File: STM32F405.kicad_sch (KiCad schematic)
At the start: 21 parts, among them SW1 SW_MEC_5E, U2 STM32F405RGTx, Y1 Crystal, Y2 Crystal

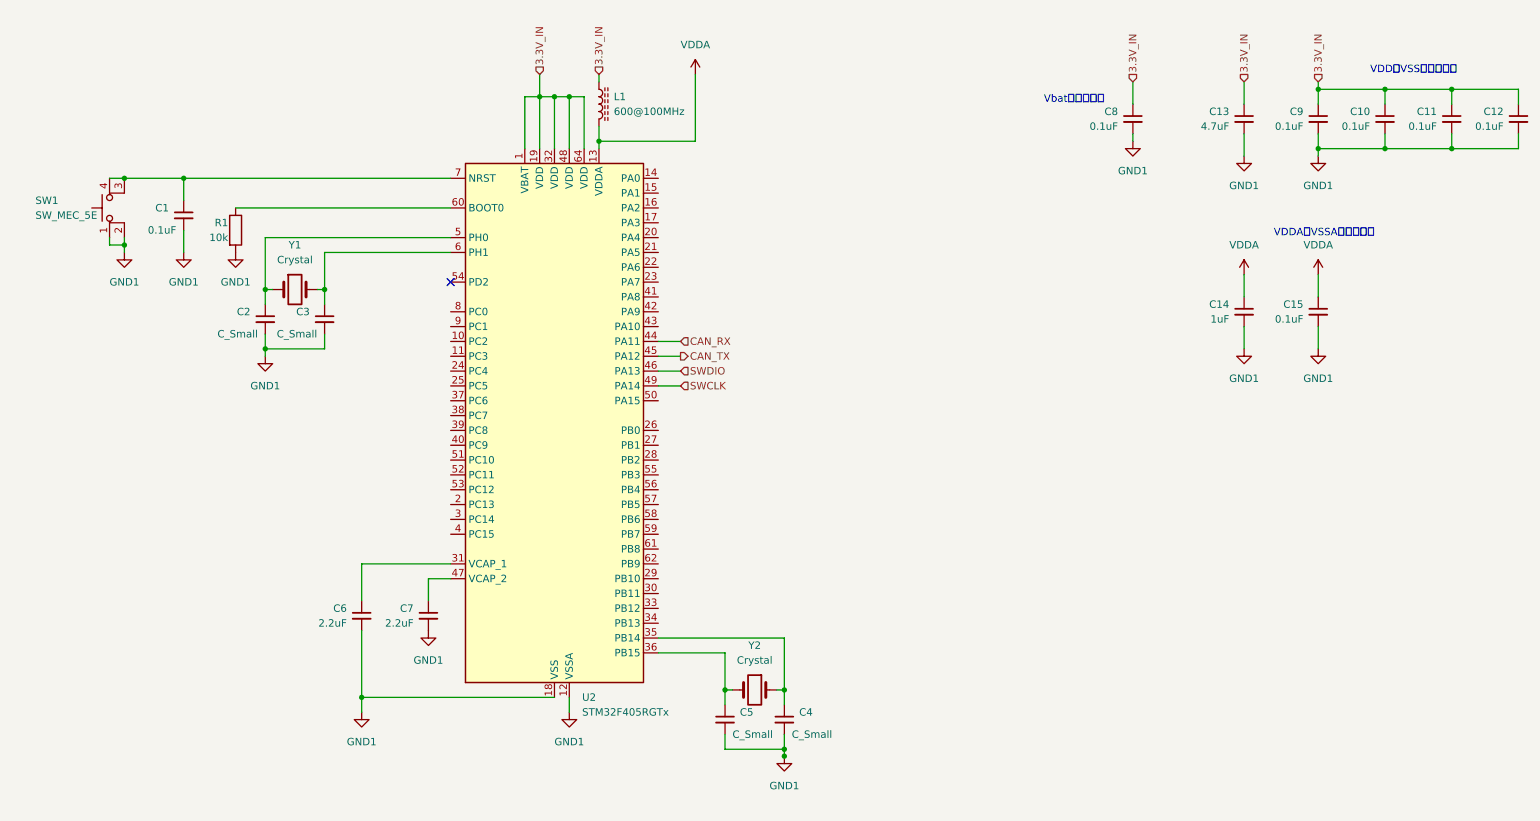
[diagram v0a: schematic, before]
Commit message: update Driver circuit
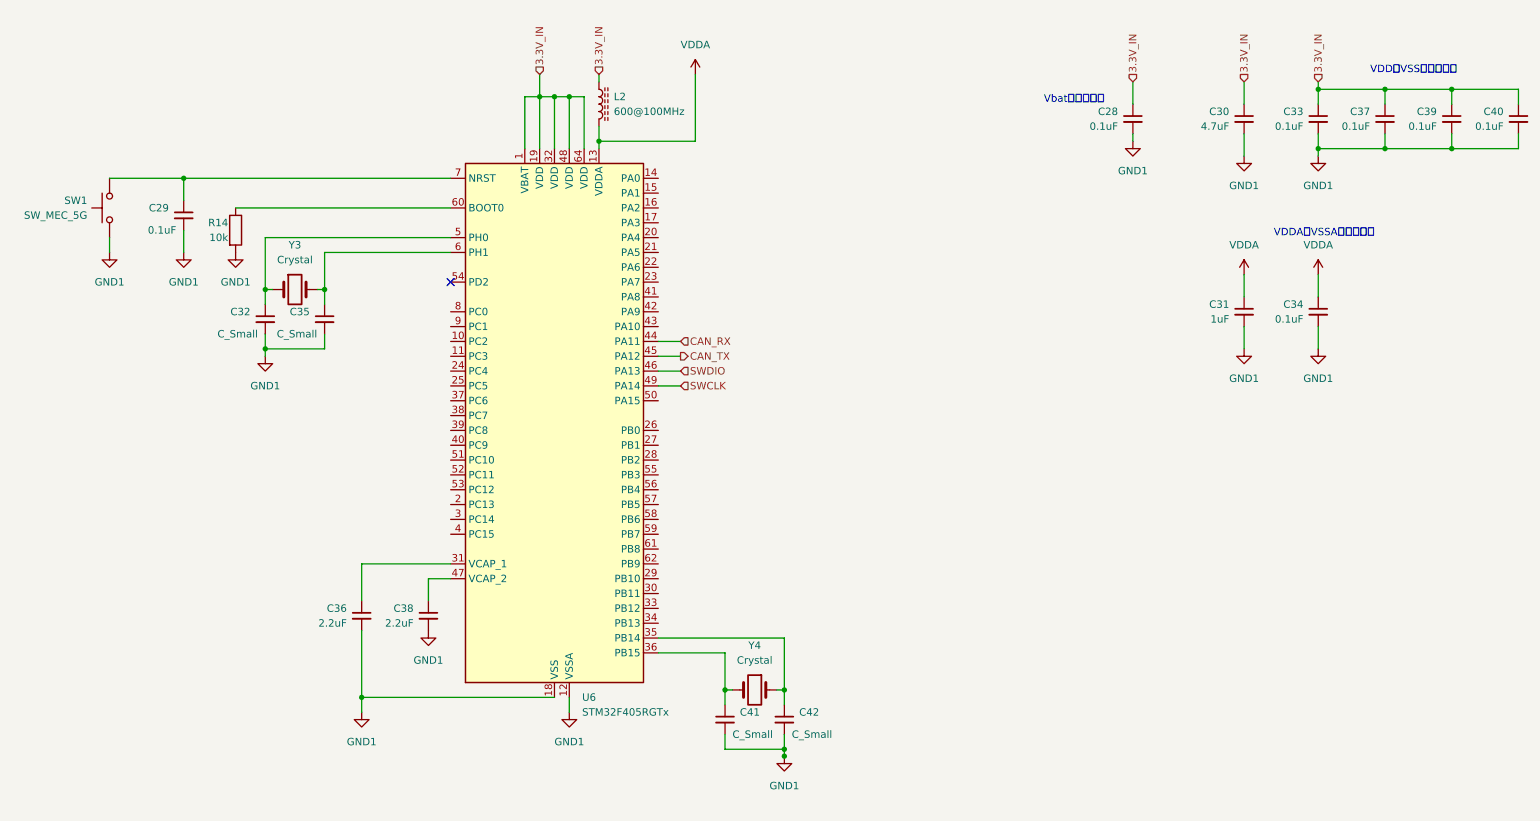
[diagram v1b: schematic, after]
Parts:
- removed SW1: SW_MEC_5E, symbol Switch:SW_MEC_5E
- added SW1: SW_MEC_5G, Button_Switch_THT:SW_PUSH_6mm, symbol Switch:SW_MEC_5G
- renumbered C8 to C28, C1 to C29, C13 to C30, C14 to C31, C2 to C32, C9 to C33, C15 to C34, C3 to C35, C6 to C36, C10 to C37, C7 to C38, C11 to C39, C12 to C40, C5 to C41, C4 to C42, L1 to L2, R1 to R14, U2 to U6, Y1 to Y3, Y2 to Y4
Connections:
- net GND1: now also SW1.1 (A), SW1.2 (A)
- net at C29.1, U6.7 (NRST): now also SW1.3 (B), SW1.4 (B)

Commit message: update parts list
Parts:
- R14: footprint (none) -> Resistor_SMD:R_1206_3216Metric_Pad1.30x1.75mm_HandSolder
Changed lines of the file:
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@@
       (effects (font (size 1.27 1.27)) (justify right))
     )
-    (property "Footprint" "" (at 56.642 53.34 90)
+    (property "Footprint" "Resistor_SMD:R_1206_3216Metric_Pad1.30x1.75mm_HandSolder" (at 56.642 53.34 90)
       (effects (font (size 1.27 1.27)) hide)
     )

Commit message: add footprint
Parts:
- C28, C29, C33, C34, C37, C39, C40: value 0.1uF -> 0.1u
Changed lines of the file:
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@@
       (effects (font (size 1.27 1.27)) (justify right))
     )
-    (property "Value" "0.1uF" (at 48.26 53.34 0)
+    (property "Value" "0.1u" (at 48.26 53.34 0)
       (effects (font (size 1.27 1.27)) (justify right))
     )
@@
       (effects (font (size 1.27 1.27)) (justify right))
     )
-    (property "Value" "0.1uF" (at 241.3 68.58 0)
+    (property "Value" "0.1u" (at 241.3 68.58 0)
       (effects (font (size 1.27 1.27)) (justify right))
     )
@@
       (effects (font (size 1.27 1.27)) (justify right))
     )
-    (property "Value" "0.1uF" (at 252.73 35.56 0)
+    (property "Value" "0.1u" (at 252.73 35.56 0)
       (effects (font (size 1.27 1.27)) (justify right))
     )
@@
       (effects (font (size 1.27 1.27)) (justify right))
     )
-    (property "Value" "0.1uF" (at 209.55 35.56 0)
+    (property "Value" "0.1u" (at 209.55 35.56 0)
       (effects (font (size 1.27 1.27)) (justify right))
     )
@@
       (effects (font (size 1.27 1.27)) (justify right))
     )
-    (property "Value" "0.1uF" (at 264.16 35.56 0)
+    (property "Value" "0.1u" (at 264.16 35.56 0)
       (effects (font (size 1.27 1.27)) (justify right))
     )
@@
       (effects (font (size 1.27 1.27)) (justify right))
     )
-    (property "Value" "0.1uF" (at 275.59 35.56 0)
+    (property "Value" "0.1u" (at 275.59 35.56 0)
       (effects (font (size 1.27 1.27)) (justify right))
     )
@@
       (effects (font (size 1.27 1.27)) (justify right))
     )
-    (property "Value" "0.1uF" (at 241.3 35.56 0)
-      (effects (font (size 1.27 1.27)) (justify right))
-    )
+    (property "Value" "0.1u" (at 241.3 35.56 0)
+      (effects (font (size 1.27 1.27)) (justify right))
+    )

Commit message: Update motor driver circuit
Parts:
- C28, C29, C33, C34, C37, C39, C40: footprint (none) -> Capacitor_SMD:C_01005_0402Metric_Pad0.57x0.30mm_HandSolder
- C30, C31, C36, C38: footprint (none) -> Capacitor_SMD:C_0603_1608Metric_Pad1.08x0.95mm_HandSolder
- L2: footprint (none) -> Resistor_SMD:R_0805_2012Metric_Pad1.20x1.40mm_HandSolder
- R14: footprint Resistor_SMD:R_1206_3216Metric_Pad1.30x1.75mm_HandSolder -> Resistor_SMD:R_0402_1005Metric_Pad0.72x0.64mm_HandSolder
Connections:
- net SWO: now reaches U6.55 (PB3)
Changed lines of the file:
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@@
+    (stroke (width 0) (type default))
+  )
+  (wire (pts (xy 130.81 95.25) (xy 134.62 95.25))
     (stroke (width 0) (type default))
   )
@@
     (effects (font (size 1.27 1.27)) (justify left))
   )
+  (hierarchical_label "SWO" (shape input) (at 134.62 95.25 0) (fields_autoplaced)
+    (effects (font (size 1.27 1.27)) (justify left))
+  )
   (hierarchical_label "SWCLK" (shape input) (at 134.62 80.01 0) (fields_autoplaced)
     (effects (font (size 1.27 1.27)) (justify left))
@@
       (effects (font (size 1.27 1.27)) (justify right))
     )
-    (property "Footprint" "" (at 231.14 34.29 0)
+    (property "Footprint" "Capacitor_SMD:C_0603_1608Metric_Pad1.08x0.95mm_HandSolder" (at 231.14 34.29 0)
       (effects (font (size 1.27 1.27)) hide)
     )
@@
       (effects (font (size 1.27 1.27)) (justify right))
     )
-    (property "Footprint" "" (at 49.53 50.8 0)
+    (property "Footprint" "Capacitor_SMD:C_01005_0402Metric_Pad0.57x0.30mm_HandSolder" (at 49.53 50.8 0)
       (effects (font (size 1.27 1.27)) hide)
     )
@@
       (effects (font (size 1.27 1.27)) (justify right))
     )
-    (property "Footprint" "" (at 243.84 67.31 0)
+    (property "Footprint" "Capacitor_SMD:C_01005_0402Metric_Pad0.57x0.30mm_HandSolder" (at 243.84 67.31 0)
       (effects (font (size 1.27 1.27)) hide)
     )
@@
       (effects (font (size 1.27 1.27)) (justify right))
     )
-    (property "Footprint" "" (at 255.27 34.29 0)
+    (property "Footprint" "Capacitor_SMD:C_01005_0402Metric_Pad0.57x0.30mm_HandSolder" (at 255.27 34.29 0)
       (effects (font (size 1.27 1.27)) hide)
     )
@@
       (effects (font (size 1.27 1.27)) (justify right))
     )
-    (property "Footprint" "" (at 80.01 119.38 0)
+    (property "Footprint" "Capacitor_SMD:C_0603_1608Metric_Pad1.08x0.95mm_HandSolder" (at 80.01 119.38 0)
       (effects (font (size 1.27 1.27)) hide)
     )
@@
       (effects (font (size 1.27 1.27)) (justify right))
     )
-    (property "Footprint" "Resistor_SMD:R_1206_3216Metric_Pad1.30x1.75mm_HandSolder" (at 56.642 53.34 90)
+    (property "Footprint" "Resistor_SMD:R_0402_1005Metric_Pad0.72x0.64mm_HandSolder" (at 56.642 53.34 90)
       (effects (font (size 1.27 1.27)) hide)
     )
@@
       (effects (font (size 1.27 1.27)) (justify right))
     )
-    (property "Footprint" "" (at 212.09 34.29 0)
+    (property "Footprint" "Capacitor_SMD:C_01005_0402Metric_Pad0.57x0.30mm_HandSolder" (at 212.09 34.29 0)
       (effects (font (size 1.27 1.27)) hide)
     )
@@
       (effects (font (size 1.27 1.27)) (justify right))
     )
-    (property "Footprint" "" (at 91.44 119.38 0)
+    (property "Footprint" "Capacitor_SMD:C_0603_1608Metric_Pad1.08x0.95mm_HandSolder" (at 91.44 119.38 0)
       (effects (font (size 1.27 1.27)) hide)
     )
@@
       (effects (font (size 1.27 1.27)) (justify right))
     )
-    (property "Footprint" "" (at 266.7 34.29 0)
+    (property "Footprint" "Capacitor_SMD:C_01005_0402Metric_Pad0.57x0.30mm_HandSolder" (at 266.7 34.29 0)
       (effects (font (size 1.27 1.27)) hide)
     )
@@
       (effects (font (size 1.27 1.27)) (justify right))
     )
-    (property "Footprint" "" (at 278.13 34.29 0)
+    (property "Footprint" "Capacitor_SMD:C_01005_0402Metric_Pad0.57x0.30mm_HandSolder" (at 278.13 34.29 0)
       (effects (font (size 1.27 1.27)) hide)
     )
@@
       (effects (font (size 1.27 1.27)) (justify right))
     )
-    (property "Footprint" "" (at 231.14 67.31 0)
+    (property "Footprint" "Capacitor_SMD:C_0603_1608Metric_Pad1.08x0.95mm_HandSolder" (at 231.14 67.31 0)
       (effects (font (size 1.27 1.27)) hide)
     )
@@
       (effects (font (size 1.27 1.27)) (justify left))
     )
-    (property "Footprint" "" (at 120.65 31.75 0)
+    (property "Footprint" "Resistor_SMD:R_0805_2012Metric_Pad1.20x1.40mm_HandSolder" (at 120.65 31.75 0)
       (effects (font (size 1.27 1.27)) hide)
     )
@@
       (effects (font (size 1.27 1.27)) (justify right))
     )
-    (property "Footprint" "" (at 243.84 34.29 0)
-      (effects (font (size 1.27 1.27)) hide)
-    )
+    (property "Footprint" "Capacitor_SMD:C_01005_0402Metric_Pad0.57x0.30mm_HandSolder" (at 243.84 34.29 0)
+      (effects (font (size 1.27 1.27)) hide)
+    )

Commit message: add logic parts
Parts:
- C28, C29, C33, C34, C37, C39, C40: footprint Capacitor_SMD:C_01005_0402Metric_Pad0.57x0.30mm_HandSolder -> Capacitor_SMD:C_0402_1005Metric_Pad0.74x0.62mm_HandSolder
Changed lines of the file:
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@@
       (effects (font (size 1.27 1.27)) (justify right))
     )
-    (property "Footprint" "Capacitor_SMD:C_01005_0402Metric_Pad0.57x0.30mm_HandSolder" (at 49.53 50.8 0)
+    (property "Footprint" "Capacitor_SMD:C_0402_1005Metric_Pad0.74x0.62mm_HandSolder" (at 49.53 50.8 0)
       (effects (font (size 1.27 1.27)) hide)
     )
@@
       (effects (font (size 1.27 1.27)) (justify right))
     )
-    (property "Footprint" "Capacitor_SMD:C_01005_0402Metric_Pad0.57x0.30mm_HandSolder" (at 243.84 67.31 0)
+    (property "Footprint" "Capacitor_SMD:C_0402_1005Metric_Pad0.74x0.62mm_HandSolder" (at 243.84 67.31 0)
       (effects (font (size 1.27 1.27)) hide)
     )
@@
       (effects (font (size 1.27 1.27)) (justify right))
     )
-    (property "Footprint" "Capacitor_SMD:C_01005_0402Metric_Pad0.57x0.30mm_HandSolder" (at 255.27 34.29 0)
+    (property "Footprint" "Capacitor_SMD:C_0402_1005Metric_Pad0.74x0.62mm_HandSolder" (at 255.27 34.29 0)
       (effects (font (size 1.27 1.27)) hide)
     )
@@
       (effects (font (size 1.27 1.27)) (justify right))
     )
-    (property "Footprint" "Capacitor_SMD:C_01005_0402Metric_Pad0.57x0.30mm_HandSolder" (at 212.09 34.29 0)
+    (property "Footprint" "Capacitor_SMD:C_0402_1005Metric_Pad0.74x0.62mm_HandSolder" (at 212.09 34.29 0)
       (effects (font (size 1.27 1.27)) hide)
     )
@@
       (effects (font (size 1.27 1.27)) (justify right))
     )
-    (property "Footprint" "Capacitor_SMD:C_01005_0402Metric_Pad0.57x0.30mm_HandSolder" (at 266.7 34.29 0)
+    (property "Footprint" "Capacitor_SMD:C_0402_1005Metric_Pad0.74x0.62mm_HandSolder" (at 266.7 34.29 0)
       (effects (font (size 1.27 1.27)) hide)
     )
@@
       (effects (font (size 1.27 1.27)) (justify right))
     )
-    (property "Footprint" "Capacitor_SMD:C_01005_0402Metric_Pad0.57x0.30mm_HandSolder" (at 278.13 34.29 0)
+    (property "Footprint" "Capacitor_SMD:C_0402_1005Metric_Pad0.74x0.62mm_HandSolder" (at 278.13 34.29 0)
       (effects (font (size 1.27 1.27)) hide)
     )
@@
       (effects (font (size 1.27 1.27)) (justify right))
     )
-    (property "Footprint" "Capacitor_SMD:C_01005_0402Metric_Pad0.57x0.30mm_HandSolder" (at 243.84 34.29 0)
-      (effects (font (size 1.27 1.27)) hide)
-    )
+    (property "Footprint" "Capacitor_SMD:C_0402_1005Metric_Pad0.74x0.62mm_HandSolder" (at 243.84 34.29 0)
+      (effects (font (size 1.27 1.27)) hide)
+    )

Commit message: update pcb
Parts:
- Y3: footprint (none) -> Crystal:Crystal_SMD_3225-4Pin_3.2x2.5mm
- Y4: footprint (none) -> Crystal:Crystal_SMD_3215-2Pin_3.2x1.5mm
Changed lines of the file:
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@@
       (effects (font (size 1.27 1.27)))
     )
-    (property "Footprint" "" (at 147.32 132.08 0)
+    (property "Footprint" "Crystal:Crystal_SMD_3215-2Pin_3.2x1.5mm" (at 147.32 132.08 0)
       (effects (font (size 1.27 1.27)) hide)
     )
@@
       (effects (font (size 1.27 1.27)))
     )
-    (property "Footprint" "" (at 68.58 63.5 0)
-      (effects (font (size 1.27 1.27)) hide)
-    )
+    (property "Footprint" "Crystal:Crystal_SMD_3225-4Pin_3.2x2.5mm" (at 68.58 63.5 0)
+      (effects (font (size 1.27 1.27)) hide)
+    )
